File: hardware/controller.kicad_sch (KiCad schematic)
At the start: 4 parts, among them J1 USB_C_Receptacle_USB2.0, U1 ESP32-WROOM-32, U2 CP2104

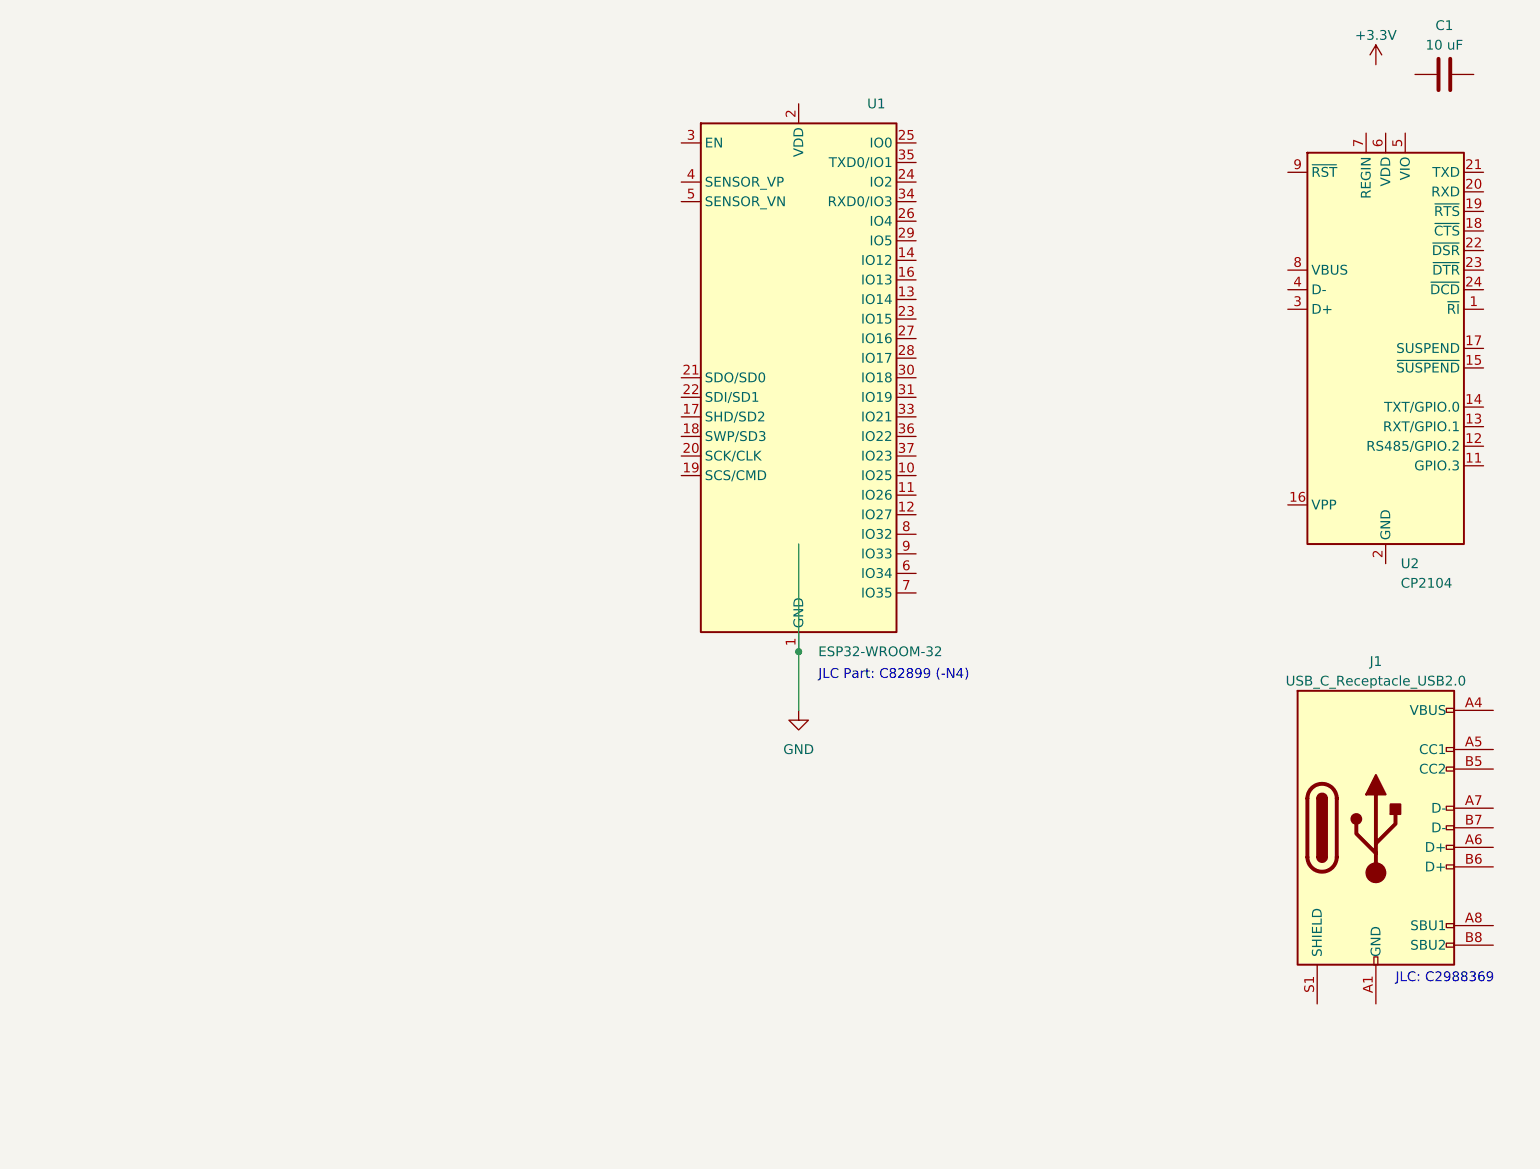
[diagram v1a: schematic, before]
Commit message: Schematic updates and initial layout
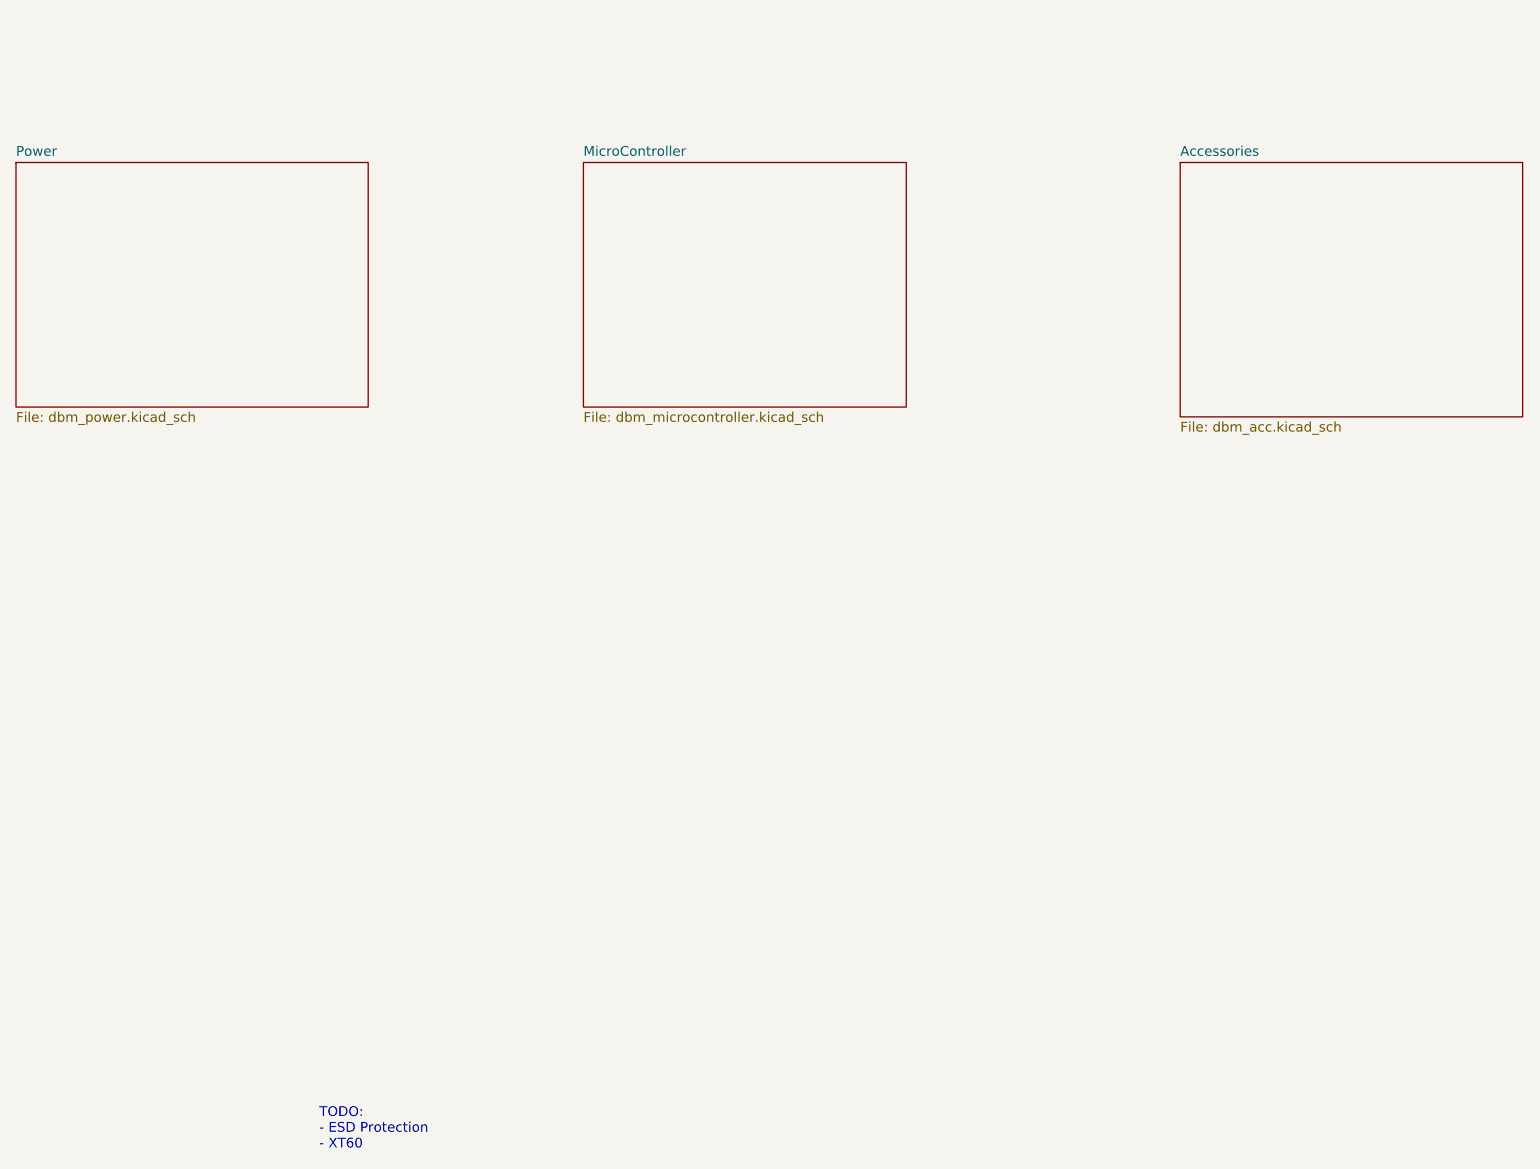
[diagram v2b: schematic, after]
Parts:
- removed C1: 10 uF, symbol Device:C
- removed J1: USB_C_Receptacle_USB2.0, Connector_USB:USB_C_Receptacle_G-Switch_GT-USB-7010ASV, symbol Connector:USB_C_Receptacle_USB2.0
- removed U1: ESP32-WROOM-32, RF_Module:ESP32-WROOM-32, symbol RF_Module:ESP32-WROOM-32
- removed U2: CP2104, Package_DFN_QFN:QFN-24-1EP_4x4mm_P0.5mm_EP2.6x2.6mm, symbol Interface_USB:CP2104
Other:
- added sheet Accessories (dbm_acc.kicad_sch)
- added sheet MicroController (dbm_microcontroller.kicad_sch)
- added sheet Power (dbm_power.kicad_sch)
- note added: "TODO: - ESD Protection - XT60"
- note removed: "JLC Part: C82899 (-N4)"
- note removed: "JLC: C2988369"
- company: (none) -> Zalgtronic
- title: (none) -> DeepBlackMagic
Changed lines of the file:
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@@
 (kicad_sch (version 20230121) (generator eeschema)
   (paper "A4")
-  (junction (at 146.05 110.49) (diameter 0) (color 0 0 0 0)
+  (title_block
+    (title "DeepBlackMagic")
+    (date "2023-05-22")
+    (rev "Rev 1")
+    (company "Zalgtronic")
   )
-  (wire (pts (xy 146.05 96.52) (xy 146.05 110.49))
-    (stroke (width 0) (type default))
-  )
-  (wire (pts (xy 146.05 110.49) (xy 146.05 118.11))
-    (stroke (width 0) (type default))
-  )
-  (text "JLC Part: C82899 (-N4)" (at 148.59 114.3 0)
+  (text "TODO:\n- ESD Protection\n- XT60\n" (at 83.82 175.26 0)
     (effects (font (size 1.27 1.27)) (justify left bottom))
   )
-  (text "JLC: C2988369\n" (at 223.52 153.67 0)
-    (effects (font (size 1.27 1.27)) (justify left bottom))
-  )
-  (symbol (lib_id "power:+3.3V") (at 220.98 34.29 0) (unit 1)
-    (in_bom yes) (on_board yes) (dnp no) (fields_autoplaced)
-    (property "Reference" "#PWR02" (at 220.98 38.1 0)
-      (effects (font (size 1.27 1.27)) hide)
+  (sheet (at 195.58 46.99) (size 44.45 33.02) (fields_autoplaced)
+    (stroke (width 0.1524) (type solid))
+    (fill (color 0 0 0 0.0000))
+    (property "Sheetname" "Accessories" (at 195.58 46.2784 0)
+      (effects (font (size 1.27 1.27)) (justify left bottom))
     )
-    (property "Value" "+3.3V" (at 220.98 30.48 0)
-      (effects (font (size 1.27 1.27)))
+    (property "Sheetfile" "dbm_acc.kicad_sch" (at 195.58 80.5946 0)
+      (effects (font (size 1.27 1.27)) (justify left top))
     )
-    (property "Footprint" "" (at 220.98 34.29 0)
-      (effects (font (size 1.27 1.27)) hide)
-    )
-    (property "Datasheet" "" (at 220.98 34.29 0)
-      (effects (font (size 1.27 1.27)) hide)
-    )
-    (pin "1")
     (instances
       (project "controller"
-        (path "/8962ec2d-787b-4db3-bd2c-cac91db8495d"
-          (reference "#PWR02") (unit 1)
-        )
+        (path "/8962ec2d-787b-4db3-bd2c-cac91db8495d" (page "4"))
       )
     )
   )
-  (symbol (lib_id "Connector:USB_C_Receptacle_USB2.0") (at 220.98 133.35 0) (unit 1)
-    (in_bom yes) (on_board yes) (dnp no) (fields_autoplaced)
-    (property "Reference" "J1" (at 220.98 111.76 0)
-      (effects (font (size 1.27 1.27)))
+  (sheet (at 44.45 46.99) (size 45.72 31.75) (fields_autoplaced)
+    (stroke (width 0.1524) (type solid))
+    (fill (color 0 0 0 0.0000))
+    (property "Sheetname" "Power" (at 44.45 46.2784 0)
+      (effects (font (size 1.27 1.27)) (justify left bottom))
     )
-    (property "Value" "USB_C_Receptacle_USB2.0" (at 220.98 114.3 0)
-      (effects (font (size 1.27 1.27)))
+    (property "Sheetfile" "dbm_power.kicad_sch" (at 44.45 79.3246 0)
+      (effects (font (size 1.27 1.27)) (justify left top))
     )
-    (property "Footprint" "Connector_USB:USB_C_Receptacle_G-Switch_GT-USB-7010ASV" (at 224.79 133.35 0)
+    (property "Field2" "" (at 44.45 46.99 0)
       (effects (font (size 1.27 1.27)) hide)
     )
-    (property "Datasheet" "https://www.usb.org/sites/default/files/documents/usb_type-c.zip" (at 224.79 133.35 0)
-      (effects (font (size 1.27 1.27)) hide)
-    )
-    (pin "A1")
-    (pin "A12")
-    (pin "A4")
-    (pin "A5")
-    (pin "A6")
-    (pin "A7")
-    (pin "A8")
-    (pin "A9")
-    (pin "B1")
-    (pin "B12")
-    (pin "B4")
-    (pin "B5")
-    (pin "B6")
-    (pin "B7")
-    (pin "B8")
-    (pin "B9")
-    (pin "S1")
     (instances
       (project "controller"
-        (path "/8962ec2d-787b-4db3-bd2c-cac91db8495d"
-          (reference "J1") (unit 1)
-        )
+        (path "/8962ec2d-787b-4db3-bd2c-cac91db8495d" (page "2"))
       )
     )
   )
-  (symbol (lib_id "power:GND") (at 146.05 118.11 0) (unit 1)
-    (in_bom yes) (on_board yes) (dnp no) (fields_autoplaced)
-    (property "Reference" "#PWR01" (at 146.05 124.46 0)
-      (effects (font (size 1.27 1.27)) hide)
+  (sheet (at 118.11 46.99) (size 41.91 31.75) (fields_autoplaced)
+    (stroke (width 0.1524) (type solid))
+    (fill (color 0 0 0 0.0000))
+    (property "Sheetname" "MicroController" (at 118.11 46.2784 0)
+      (effects (font (size 1.27 1.27)) (justify left bottom))
     )
-    (property "Value" "GND" (at 146.05 123.19 0)
-      (effects (font (size 1.27 1.27)))
+    (property "Sheetfile" "dbm_microcontroller.kicad_sch" (at 118.11 79.3246 0)
+      (effects (font (size 1.27 1.27)) (justify left top))
     )
-    (property "Footprint" "" (at 146.05 118.11 0)
-      (effects (font (size 1.27 1.27)) hide)
-    )
-    (property "Datasheet" "" (at 146.05 118.11 0)
-      (effects (font (size 1.27 1.27)) hide)
-    )
-    (pin "1")
     (instances
       (project "controller"
-        (path "/8962ec2d-787b-4db3-bd2c-cac91db8495d"
-          (reference "#PWR01") (unit 1)
-        )
+        (path "/8962ec2d-787b-4db3-bd2c-cac91db8495d" (page "3"))
       )
     )
-  )
-  (symbol (lib_id "Interface_USB:CP2104") (at 222.25 71.12 0) (unit 1)
-    (in_bom yes) (on_board yes) (dnp no) (fields_autoplaced)
-    (property "Reference" "U2" (at 224.2059 99.06 0)
-      (effects (font (size 1.27 1.27)) (justify left))
-    )
-    (property "Value" "CP2104" (at 224.2059 101.6 0)
-      (effects (font (size 1.27 1.27)) (justify left))
-    )
-    (property "Footprint" "Package_DFN_QFN:QFN-24-1EP_4x4mm_P0.5mm_EP2.6x2.6mm" (at 251.46 123.19 0)
-      (effects (font (size 1.27 1.27)) (justify left) hide)
-    )
-    (property "Datasheet" "https://www.silabs.com/documents/public/data-sheets/cp2104.pdf" (at 327.66 60.96 0)
-      (effects (font (size 1.27 1.27)) hide)
-    )
-    (pin "1")
-    (pin "10")
-    (pin "11")
-    (pin "12")
-    (pin "13")
-    (pin "14")
-    (pin "15")
-    (pin "16")
-    (pin "17")
-    (pin "18")
-    (pin "19")
-    (pin "2")
-    (pin "20")
-    (pin "21")
-    (pin "22")
-    (pin "23")
-    (pin "24")
-    (pin "25")
-    (pin "3")
-    (pin "4")
-    (pin "5")
-    (pin "6")
-    (pin "7")
-    (pin "8")
-    (pin "9")
-    (instances
-      (project "controller"
-        (path "/8962ec2d-787b-4db3-bd2c-cac91db8495d"
-          (reference "U2") (unit 1)
-        )
-      )
-    )
-  )
-  (symbol (lib_id "Device:C") (at 229.87 35.56 270) (unit 1)
-    (in_bom yes) (on_board yes) (dnp no) (fields_autoplaced)
-    (property "Reference" "C1" (at 229.87 29.21 90)
-      (effects (font (size 1.27 1.27)))
-    )
-    (property "Value" "10 uF" (at 229.87 31.75 90)
-      (effects (font (size 1.27 1.27)))
-    )
-    (property "Footprint" "" (at 226.06 36.5252 0)
-      (effects (font (size 1.27 1.27)) hide)
-    )
-    (property "Datasheet" "~" (at 229.87 35.56 0)
-      (effects (font (size 1.27 1.27)) hide)
-    )
-    (pin "1")
-    (pin "2")
-    (instances
-      (project "controller"
-        (path "/8962ec2d-787b-4db3-bd2c-cac91db8495d"
-          (reference "C1") (unit 1)
-        )
-      )
-    )
-  )
-  (symbol (lib_id "RF_Module:ESP32-WROOM-32") (at 146.05 74.93 0) (unit 1)
-    (in_bom yes) (on_board yes) (dnp no)
-    (property "Reference" "U1" (at 154.94 39.37 0)
-      (effects (font (size 1.27 1.27)) (justify left))
-    )
-    (property "Value" "ESP32-WROOM-32" (at 148.59 110.49 0)
-      (effects (font (size 1.27 1.27)) (justify left))
-    )
-    (property "Footprint" "RF_Module:ESP32-WROOM-32" (at 146.05 113.03 0)
-      (effects (font (size 1.27 1.27)) hide)
-    )
-    (property "Datasheet" "https://www.espressif.com/sites/default/files/documentation/esp32-wroom-32_datasheet_en.pdf" (at 138.43 73.66 0)
-      (effects (font (size 1.27 1.27)) hide)
-    )
-    (pin "1")
-    (pin "10")
-    (pin "11")
-    (pin "12")
-    (pin "13")
-    (pin "14")
-    (pin "15")
-    (pin "16")
-    (pin "17")
-    (pin "18")
-    (pin "19")
-    (pin "2")
-    (pin "20")
-    (pin "21")
-    (pin "22")
-    (pin "23")
-    (pin "24")
-    (pin "25")
-    (pin "26")
-    (pin "27")
-    (pin "28")
-    (pin "29")
-    (pin "3")
-    (pin "30")
-    (pin "31")
-    (pin "32")
-    (pin "33")
-    (pin "34")
-    (pin "35")
-    (pin "36")
-    (pin "37")
-    (pin "38")
-    (pin "39")
-    (pin "4")
-    (pin "5")
-    (pin "6")
-    (pin "7")
-    (pin "8")
-    (pin "9")
-    (instances
-      (project "controller"
-        (path "/8962ec2d-787b-4db3-bd2c-cac91db8495d"
-          (reference "U1") (unit 1)
-        )
-      )
-    )
